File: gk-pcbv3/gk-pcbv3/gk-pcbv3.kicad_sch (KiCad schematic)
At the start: 33 parts, among them J1 USB_C_Receptacle_USB2.0, J14 USB_A, J2 Conn_01x02, J7 Conn_01x02, J8 Conn_ARM_JTAG_SWD_10, U1 WE-TVS-82400102, U10 MAX17048, U2 MCP73831-2-OT, U23 WE-TVS-82400102, U24 TPS2051CDBV

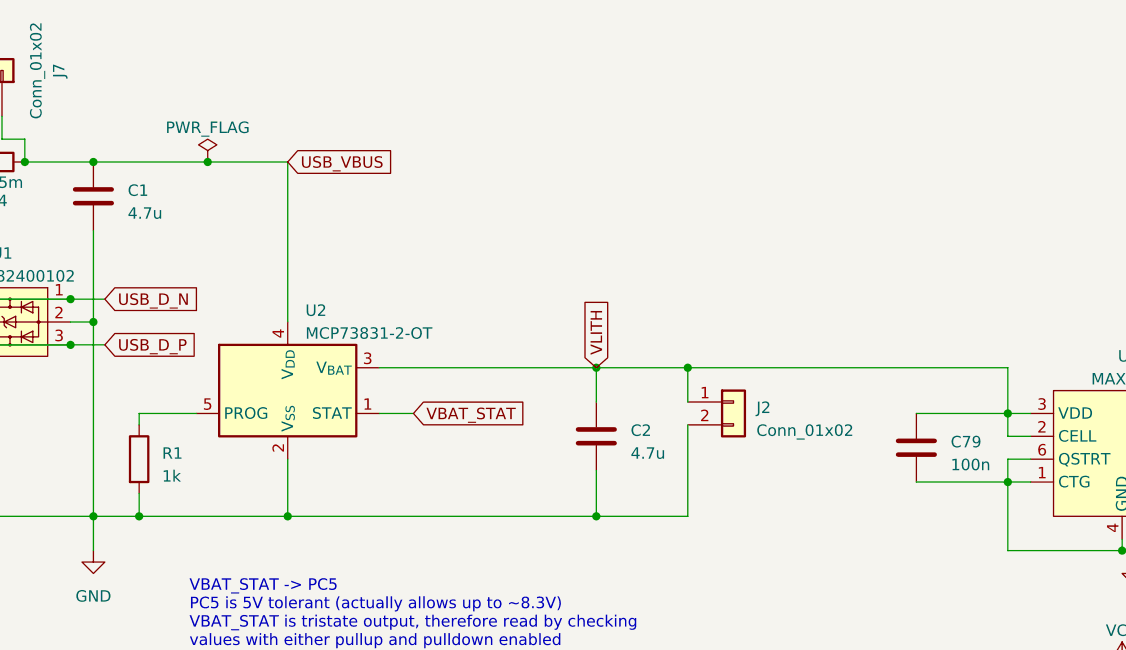
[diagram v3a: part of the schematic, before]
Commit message: add diode into battery charger
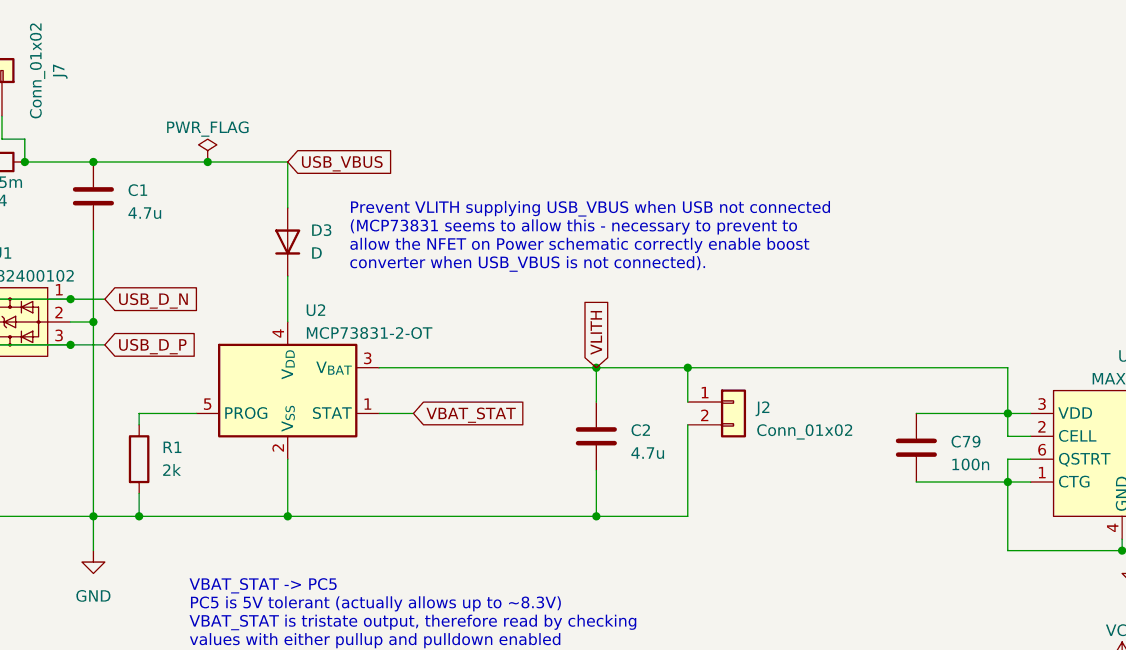
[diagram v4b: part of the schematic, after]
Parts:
- added D3: D, Diode_SMD:D_SOD-128, symbol Device:D
- R1: value 1k -> 2k
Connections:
- net USB_VBUS: now also D3.2 (A); no longer U2.4 (V_{DD})
- new net: D3.1 (K), U2.4 (V_{DD})
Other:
- note added: "Prevent VLITH supplying USB_VBUS when USB not connected (MCP73831 seems to allow this - necessary to prevent to allow the NFET on Power schematic correctly enable boost converter when USB_VBUS is not connected)."
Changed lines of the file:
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@@
-	(wire
-		(pts
-			(xy 102.87 33.02) (xy 102.87 50.8)
-		)
-		(stroke
-			(width 0)
-			(type default)
-		)
-	)
 	(wire
 		(pts
@@
 	(wire
 		(pts
+			(xy 102.87 45.72) (xy 102.87 50.8)
+		)
+		(stroke
+			(width 0)
+			(type default)
+		)
+	)
+	(wire
+		(pts
 			(xy 260.35 88.9) (xy 262.89 88.9)
 		)
@@
 		(pts
 			(xy 41.91 19.05) (xy 54.61 19.05)
+		)
+		(stroke
+			(width 0)
+			(type default)
+		)
+	)
+	(wire
+		(pts
+			(xy 102.87 33.02) (xy 102.87 38.1)
 		)
 		(stroke
@@
 			(font
 				(face "Courier New")
+				(size 1.27 1.27)
+			)
+			(justify left)
+		)
+	)
+	(text "Prevent VLITH supplying USB_VBUS when USB not connected\n(MCP73831 seems to allow this - necessary to prevent to\nallow the NFET on Power schematic correctly enable boost\nconverter when USB_VBUS is not connected)."
+		(exclude_from_sim no)
+		(at 109.728 41.402 0)
+		(effects
+			(font
 				(size 1.27 1.27)
 			)
@@
 		(fields_autoplaced yes)
 		(property "Reference" "R1"
-			(at 88.9 65.405 0)
-			(effects
-				(font
-					(size 1.27 1.27)
-				)
-				(justify left)
-			)
-		)
-		(property "Value" "1k"
-			(at 88.9 67.945 0)
+			(at 88.9 64.7699 0)
+			(effects
+				(font
+					(size 1.27 1.27)
+				)
+				(justify left)
+			)
+		)
+		(property "Value" "2k"
+			(at 88.9 67.3099 0)
 			(effects
 				(font
@@
 					(unit 1)
 				)
+			)
+		)
+	)
+	(symbol
+		(lib_id "Device:D")
+		(at 102.87 41.91 90)
+		(unit 1)
+		(exclude_from_sim no)
+		(in_bom yes)
+		(on_board yes)
+		(dnp no)
+		(fields_autoplaced yes)
+		(property "Reference" "D3"
+			(at 105.41 40.6399 90)
+			(effects
+				(font
+					(size 1.27 1.27)
+				)
+				(justify right)
+			)
+		)
+		(property "Value" "D"
+			(at 105.41 43.1799 90)
+			(effects
+				(font
+					(size 1.27 1.27)
+				)
+				(justify right)
+			)
+		)
+		(property "Footprint" "Diode_SMD:D_SOD-128"
+			(at 102.87 41.91 0)
+			(effects
+				(font
+					(size 1.27 1.27)
+				)
+				(hide yes)
+			)
+		)
+		(property "Datasheet" "~"
+			(at 102.87 41.91 0)
+			(effects
+				(font
+					(size 1.27 1.27)
+				)
+				(hide yes)
+			)
+		)
+		(property "Description" ""
+			(at 102.87 41.91 0)
+			(effects
+				(font
+					(size 1.27 1.27)
+				)
+				(hide yes)
+			)
+		)
+		(property "Sim.Device" "D"
+			(at 102.87 41.91 0)
+			(effects
+				(font
+					(size 1.27 1.27)
+				)
+				(hide yes)
+			)
+		)
+		(property "Sim.Pins" "1=K 2=A"
+			(at 102.87 41.91 0)
+			(effects
+				(font
+					(size 1.27 1.27)
+				)
+				(hide yes)
+			)
+		)
+		(pin "1"
+		)
+		(pin "2"
+		)
+		(instances
+			(project "gk-pcbv3"
+				(path "/08730ac6-6084-459f-bdf1-86b322355ede"
+					(reference "D3")
+					(unit 1)
+				)

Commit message: add comment for getting battery to work
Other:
- note added: "TODO: either rework circuit or put VLITH label here on pin 4 of MCP73831"
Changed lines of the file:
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@@
+		)
+	)
+	(text "TODO: either rework circuit or put VLITH label here on pin 4 of MCP73831"
+		(exclude_from_sim no)
+		(at 176.53 48.768 0)
+		(effects
+			(font
+				(size 1.27 1.27)
+			)
 		)
 	)

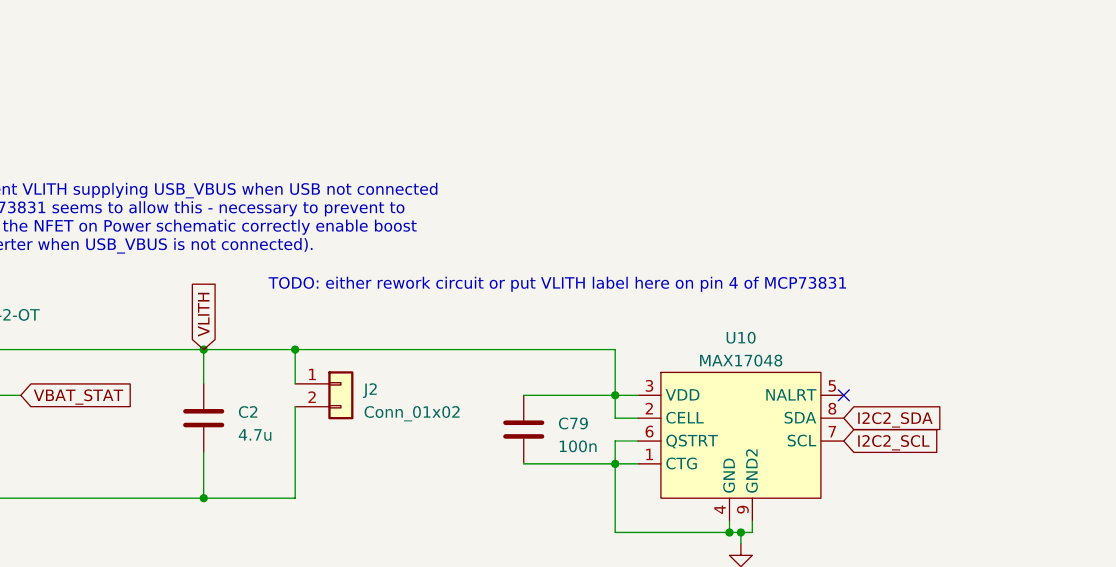
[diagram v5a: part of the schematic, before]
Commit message: begin wifi integration
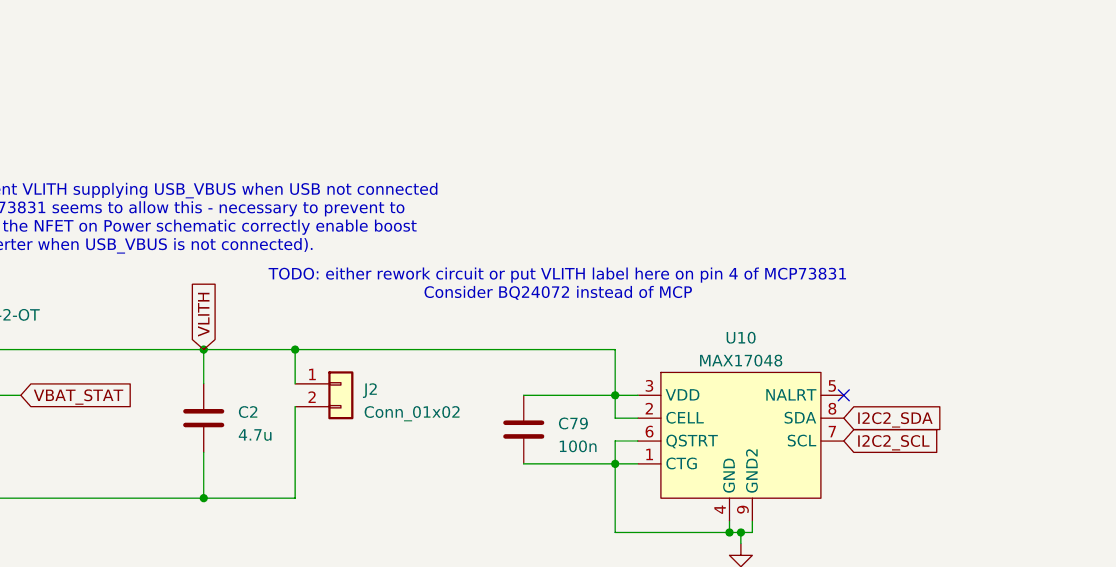
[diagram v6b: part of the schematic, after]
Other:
- note added: "TODO: either rework circuit or put VLITH label here on pin 4 of MCP73831 Consider BQ24072 instead of MCP"
- note removed: "TODO: either rework circuit or put VLITH label here on pin 4 of MCP73831"
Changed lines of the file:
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@@
 		)
 	)
-	(text "TODO: either rework circuit or put VLITH label here on pin 4 of MCP73831"
+	(text "TODO: either rework circuit or put VLITH label here on pin 4 of MCP73831\nConsider BQ24072 instead of MCP"
 		(exclude_from_sim no)
 		(at 176.53 48.768 0)

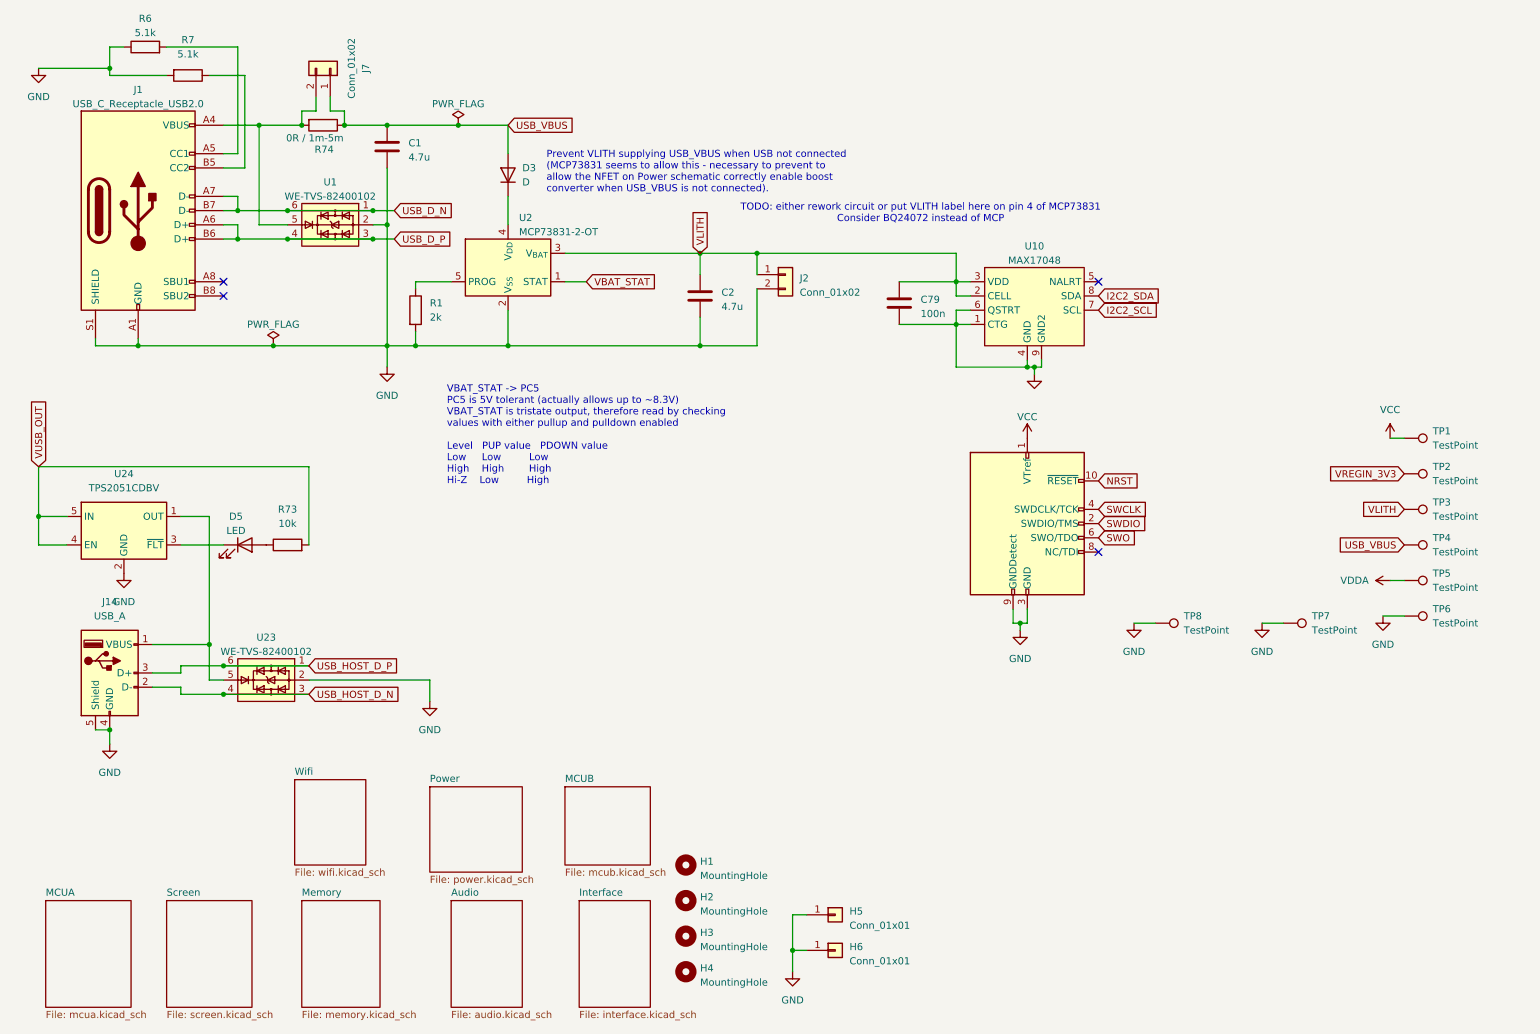
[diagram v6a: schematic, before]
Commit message: update schematics for new vreg design
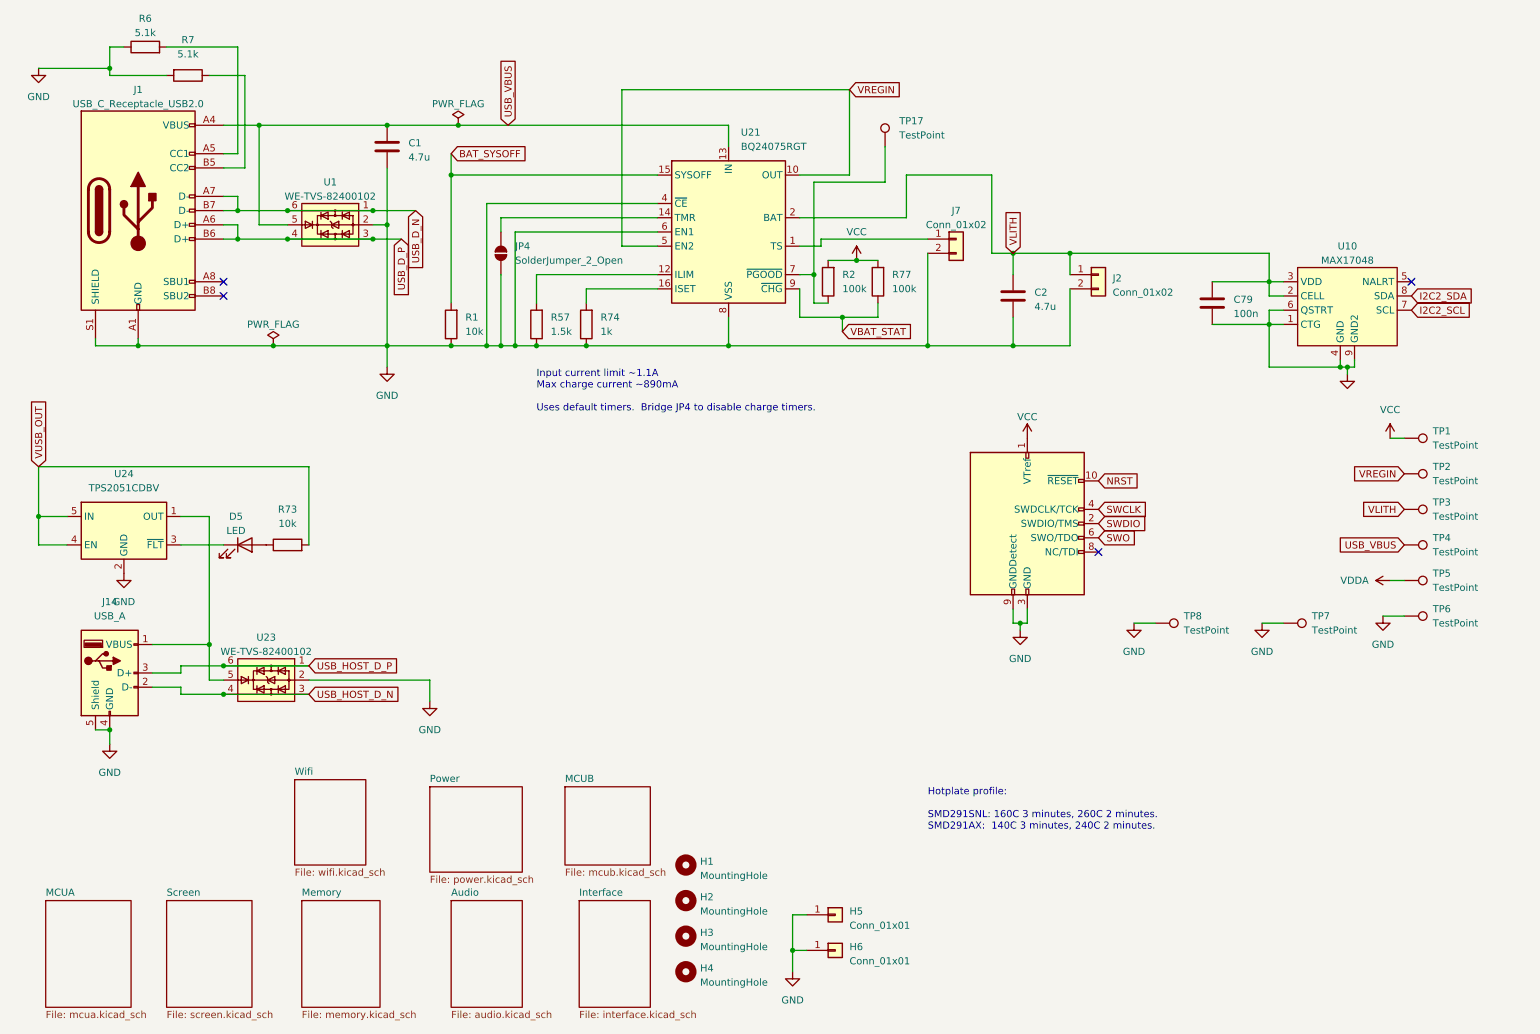
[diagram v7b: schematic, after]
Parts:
- removed D3: D, Diode_SMD:D_SOD-128, symbol Device:D
- removed U2: MCP73831-2-OT, Package_TO_SOT_SMD:SOT-23-5, symbol Battery_Management:MCP73831-2-OT
- added JP4: SolderJumper_2_Open, symbol Jumper:SolderJumper_2_Open
- added R2, R77: 100k, Resistor_SMD:R_0603_1608Metric, symbol Device:R
- added R57: 1.5k, Resistor_SMD:R_0603_1608Metric, symbol Device:R
- added TP17: TestPoint, TestPoint:TestPoint_Pad_D1.0mm, symbol Connector:TestPoint
- added U21: BQ24075RGT, Package_DFN_QFN:VQFN-16-1EP_3x3mm_P0.5mm_EP1.6x1.6mm, symbol Battery_Management:BQ24075RGT
- J7: footprint Connector_PinHeader_2.54mm:PinHeader_1x02_P2.54mm_Vertical -> Connector_JST:JST_XH_S2B-XH-A_1x02_P2.50mm_Horizontal
- R1: value 2k -> 10k
- R74: value 0R / 1m-5m -> 1k; footprint Resistor_SMD:R_2512_6332Metric -> Resistor_SMD:R_0603_1608Metric
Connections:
- net GND: now also J7.2 (Pin_2), R1.1, R74.1, JP4.1 (A), R57.1, U21.17 (VSS), U21.4 (~{CE}), U21.6 (EN1), U21.8 (VSS); no longer R1.2
- net USB_VBUS: now also J1.A4 (VBUS), J1.A9 (VBUS), J1.B4 (VBUS), J1.B9 (VBUS), U1.5, U21.13 (IN); no longer J7.1 (Pin_1), R74.1
- net VBAT_STAT: now also R77.1, U21.9 (~{CHG})
- net VCC: now also R2.2, R77.2
- net VLITH: now also U21.2 (BAT), U21.3 (BAT)
- net VREGIN_3V3 renamed VREGIN
- net VREGIN: now also U21.10 (OUT), U21.11 (OUT), U21.5 (EN2)
- new net: R2.1, TP17.1, U21.7 (~{PGOOD})
- new net: R57.2, U21.12 (ILIM)
- new net: R74.2, U21.16 (ISET)
- new net: J7.1 (Pin_1), U21.1 (TS)
- new net: JP4.2 (B), U21.14 (TMR)
- new net BAT_SYSOFF: R1.2, U21.15 (SYSOFF)
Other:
- note added: "Hotplate profile: SMD291SNL: 160C 3 minutes, 260C 2 minutes. SMD291AX: 140C 3 minutes, 240C 2 minutes."
- note added: "Input current limit ~1.1A Max charge current ~890mA Uses default timers. Bridge JP4 to disable charge timers."
- note removed: "Prevent VLITH supplying USB_VBUS when USB not connected (MCP73831 seems to allow this - necessary to prevent to allow the NFET on Power schematic correctly enable boost converter when USB_VBUS is not connected)."
- note removed: "TODO: either rework circuit or put VLITH label here on pin 4 of MCP73831 Consider BQ24072 instead of MCP"
- note removed: "VBAT_STAT -> PC5 PC5 is 5V tolerant (actually allows up to ~8.3V) VBAT_STAT is tristate output, therefore read by checking values with either pullup and pulldown enabled Level PUP value PDOWN value Low Low Low High High High Hi-Z Low High"
- moved on the sheet: C2, C79, J2, U10
